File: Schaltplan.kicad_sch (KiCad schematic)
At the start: 19 parts, among them K1 Relay, P1 USB Port vorheriger, P2 USB Port nächster, P4 USB Port Laden, U1 DC DC Wandler, U2 DC DC Wandler, U3 Digitaler Poti, U4 Display, U5 DC DC Wandler, U6 Digitaler Poti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

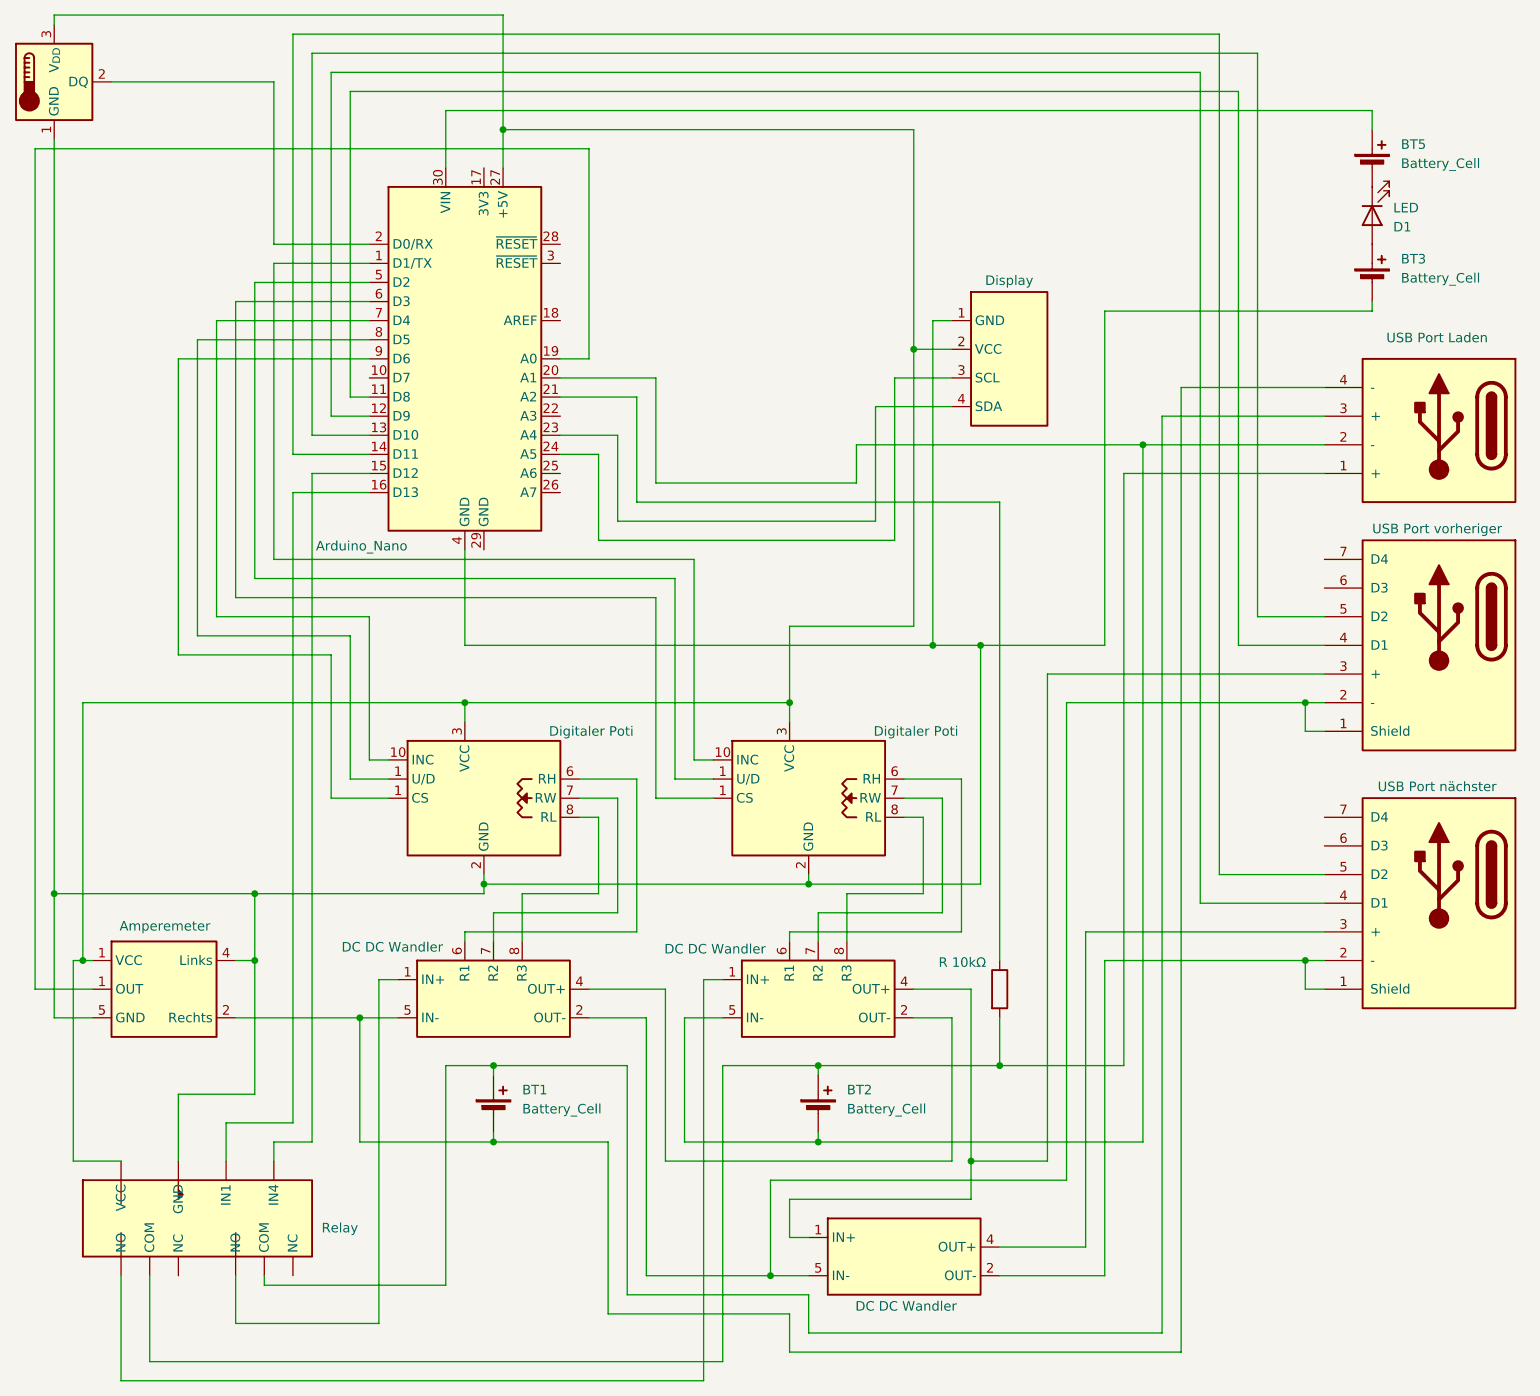
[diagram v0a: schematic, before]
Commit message: Removed extra batteries
Co-authored-by: JumpStone <hi@jumpstone4477.de>
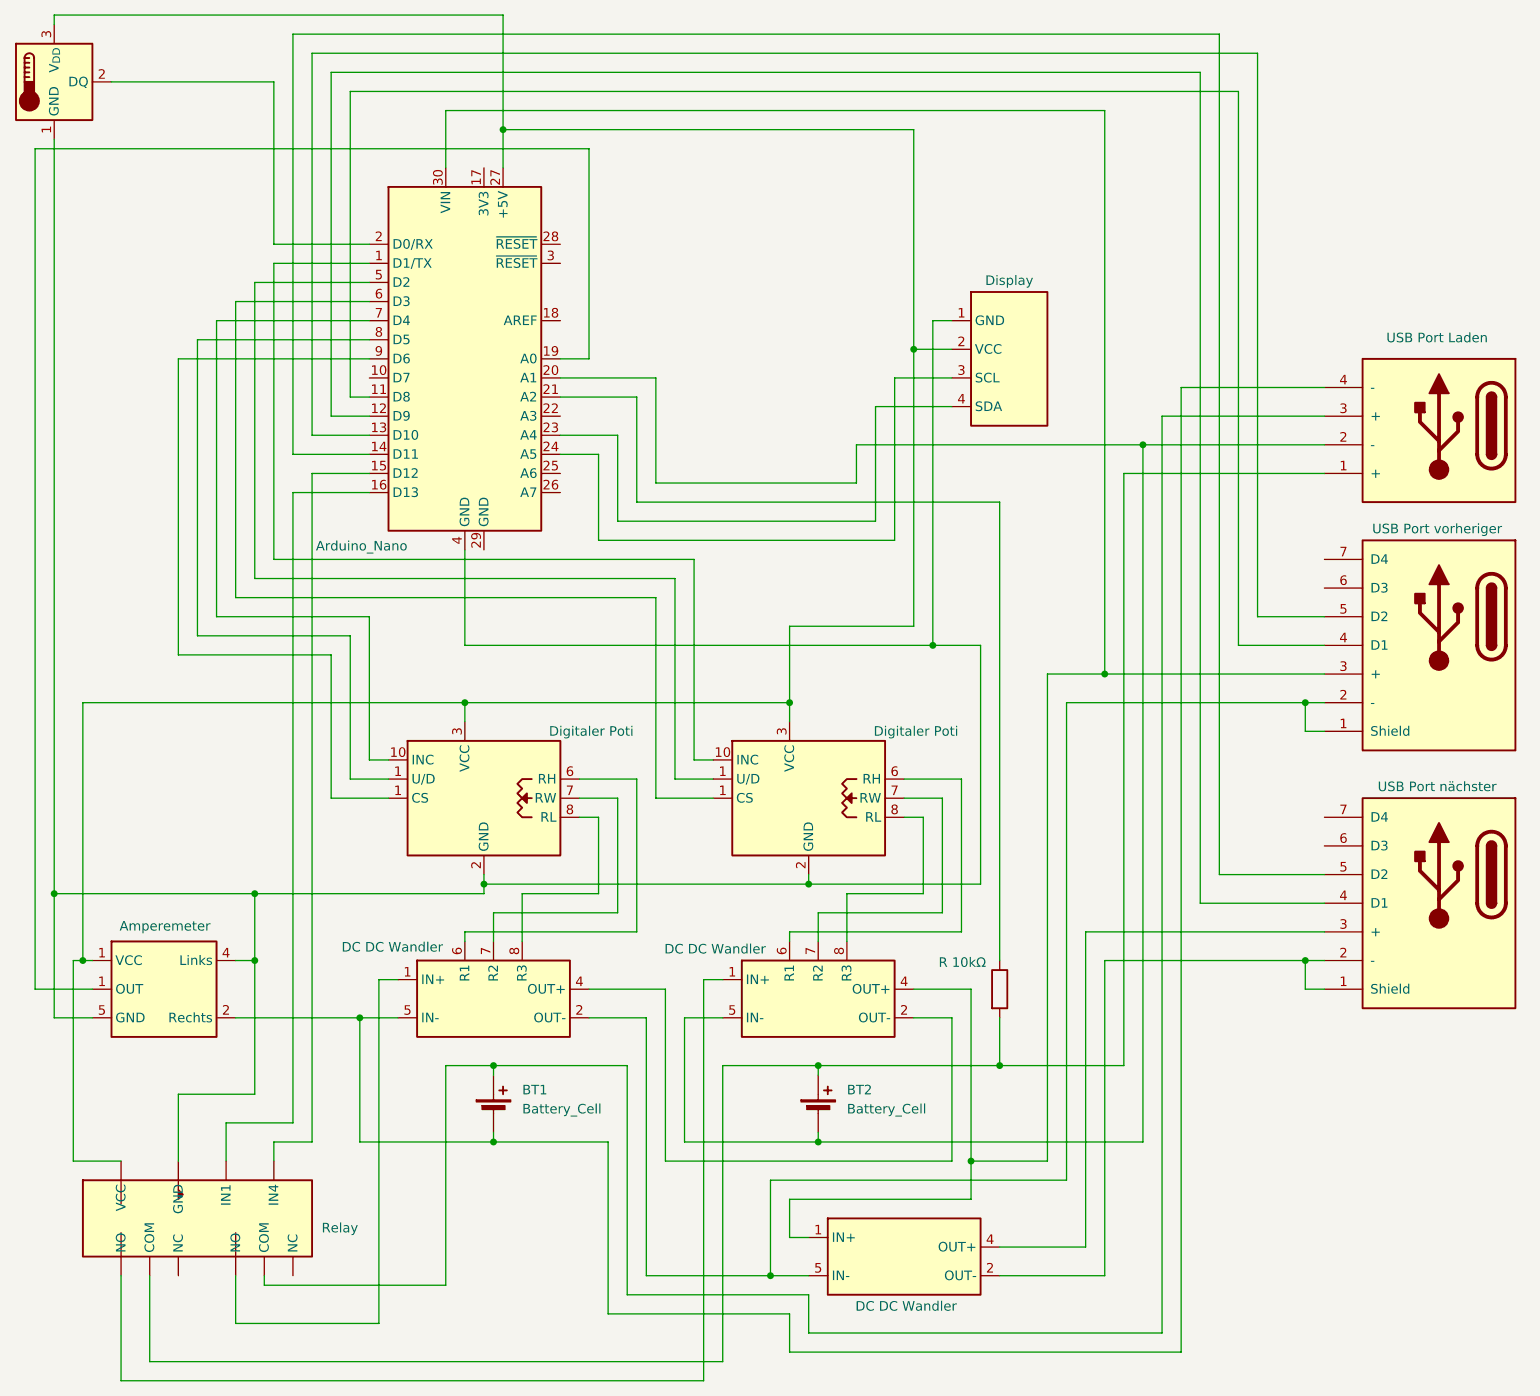
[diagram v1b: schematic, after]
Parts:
- removed BT3, BT5: Battery_Cell, symbol Device:Battery_Cell
- removed D1: LED, symbol Device:LED
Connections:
- net at A1.30 (VIN): now also P1.3 (+), U1.4 (OUT+), U5.1 (IN+)
- net at K1. (NC): now also A1.16 (D13)

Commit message: Color stuff
Co-authored-by: JumpStone <hi@jumpstone4477.de>
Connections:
- net at K1. (NC): now also A1.16 (D13)

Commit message: Color stuff cable ahhh
Co-authored-by: JumpStone <hi@jumpstone4477.de>
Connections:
- net at K1. (NC): now also A1.16 (D13)
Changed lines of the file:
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@@
 			(width 0)
 			(type default)
+			(color 255 0 0 1)
 		)
 	)

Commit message: Color stuff cable again
Co-authored-by: JumpStone <hi@jumpstone4477.de>
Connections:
- net at K1. (NC): now also A1.16 (D13)
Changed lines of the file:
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@@
 			(width 0)
 			(type default)
+			(color 0 0 0 1)
 		)
 	)
